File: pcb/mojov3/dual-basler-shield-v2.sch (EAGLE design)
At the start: 6 parts, among them Y1 SI514

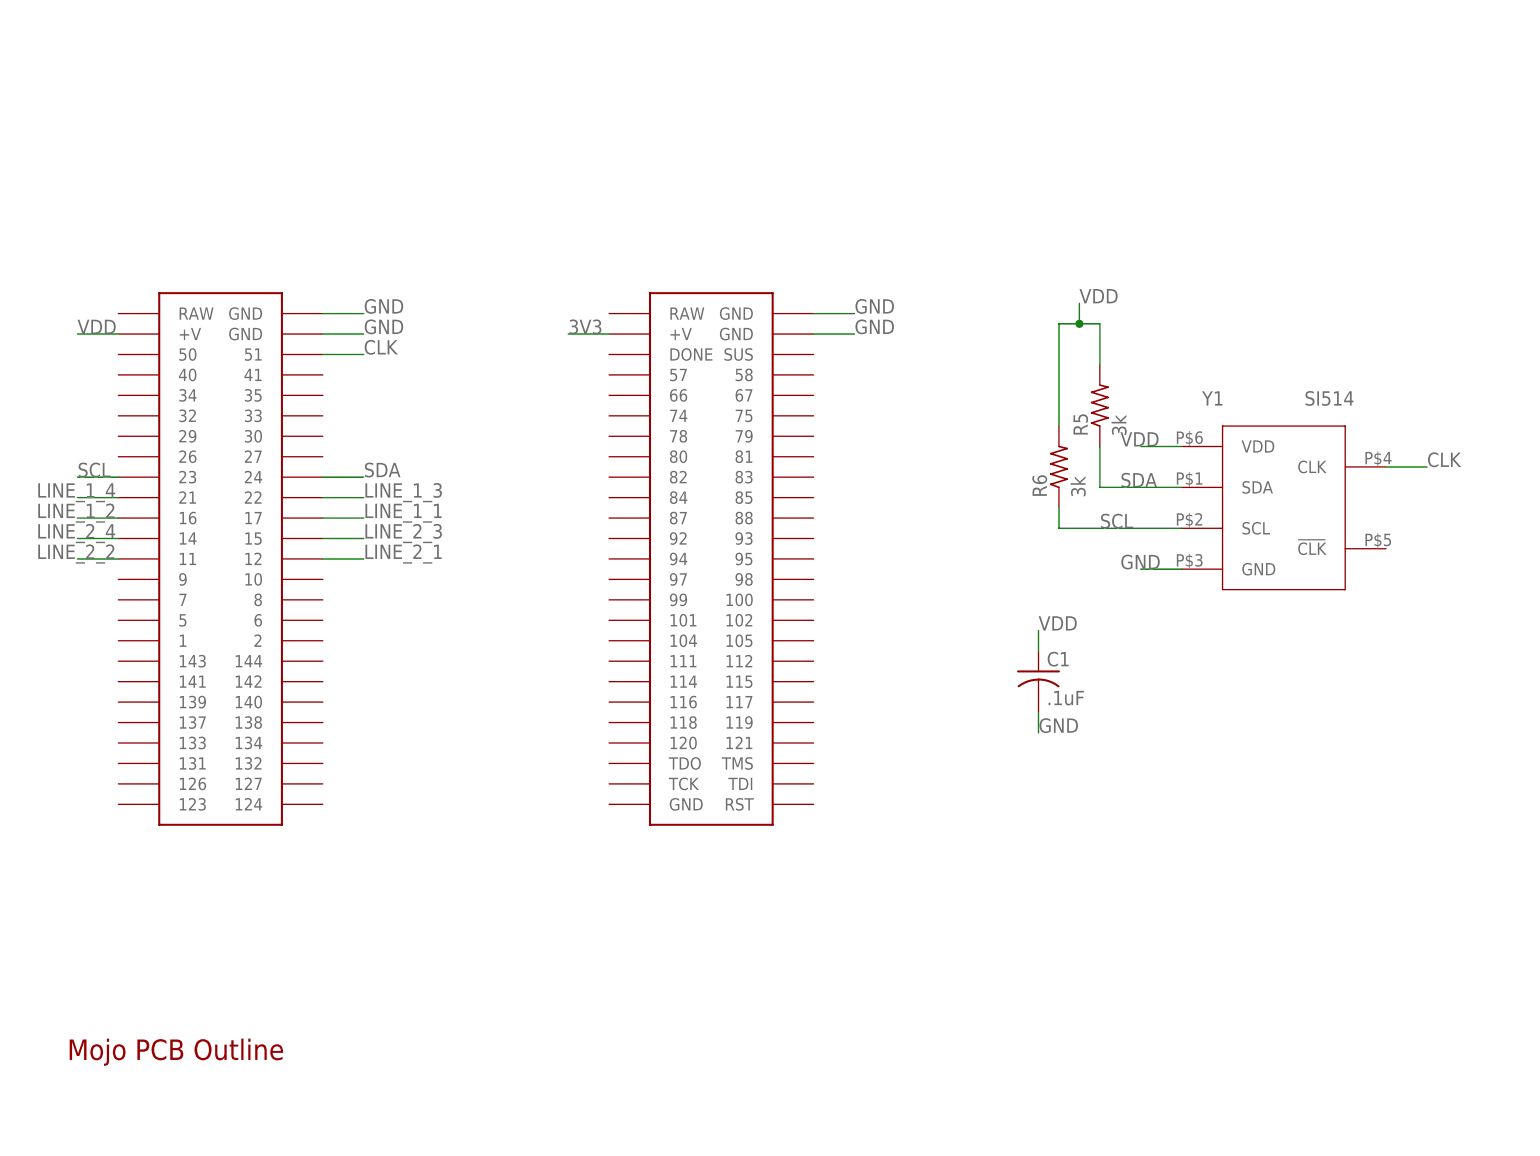
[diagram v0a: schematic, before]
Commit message: routed new mojo board
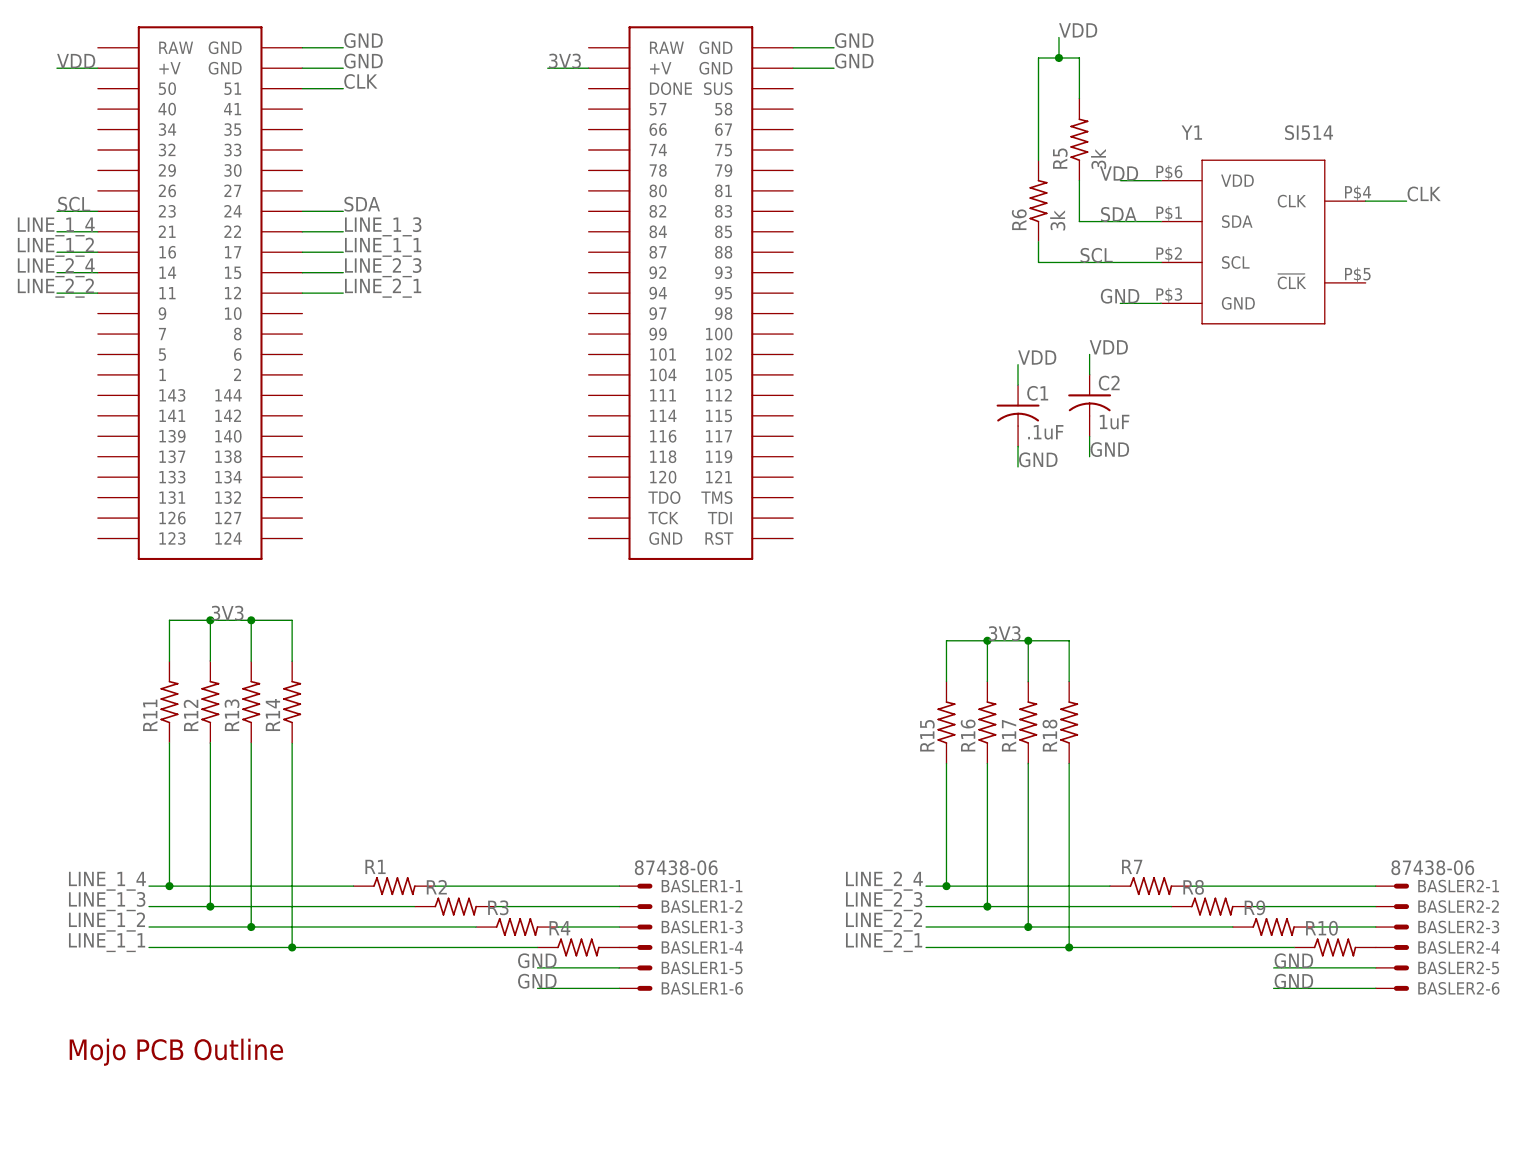
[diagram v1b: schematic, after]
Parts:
- added BASLER1, BASLER2: 87438-06, con-molex:87438-06
- added C2: 1uF, rcl:C-USC0603
- added R1, R10, R11, R12, R13, R14, R15, R16, R17, R18, R2, R3, R4, R7, R8, R9: (no value), resistor:R-US_R0603
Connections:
- new net N$1: BASLER1-1.S, R1.2
- new net N$2: BASLER1-2.S, R2.2
- new net N$3: BASLER1-3.S, R3.2
- new net N$4: BASLER1-4.S, R4.2
- new net N$5: BASLER2-1.S, R7.2
- new net N$6: BASLER2-2.S, R8.2
- new net N$7: BASLER2-3.S, R9.2
- new net N$8: BASLER2-4.S, R10.2
- net 3V3: now also R11.2, R12.2, R13.2, R14.2, R15.2, R16.2, R17.2, R18.2
- net GND: now also BASLER1-5.S, BASLER1-6.S, BASLER2-5.S, BASLER2-6.S, C2.2
- net LINE_1_1: now also R14.1, R4.1
- net LINE_1_2: now also R13.1, R3.1
- net LINE_1_3: now also R12.1, R2.1
- net LINE_1_4: now also R1.1, R11.1
- net LINE_2_1: now also R10.1, R18.1
- net LINE_2_2: now also R17.1, R9.1
- net LINE_2_3: now also R16.1, R8.1
- net LINE_2_4: now also R15.1, R7.1
- net VDD: now also C2.1
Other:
- moved on the sheet: C1, R5, R6, Y1

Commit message: finished basler shield v2
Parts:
- added LINE_1_1, LINE_1_2, LINE_1_3, LINE_1_4, LINE_2_1, LINE_2_2, LINE_2_3, LINE_2_4, TP_GND: TPTP16R, testpad:TPTP16R
- added R19, R20, R21, R22, R23, R24, R25, R26: (no value), rcl:R-US_R0603
- R1, R10, R11, R12, R13, R14, R15, R16, R17, R18, R2, R3, R4, R7, R8, R9: device resistor:R-US_R0603 -> rcl:R-US_R0603
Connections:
- net GND: now also R19.1, R20.1, R21.1, R22.1, R23.1, R24.1, R25.1, R26.1, TP_GND.TP
- net LINE_1_1: now also LINE_1_1.TP, R22.2
- net LINE_1_2: now also LINE_1_2.TP, R21.2
- net LINE_1_3: now also LINE_1_3.TP, R20.2
- net LINE_1_4: now also LINE_1_4.TP, R19.2
- net LINE_2_1: now also LINE_2_1.TP, R26.2
- net LINE_2_2: now also LINE_2_2.TP, R25.2
- net LINE_2_3: now also LINE_2_3.TP, R24.2
- net LINE_2_4: now also LINE_2_4.TP, R23.2
